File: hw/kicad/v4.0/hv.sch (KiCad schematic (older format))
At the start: 13 parts, among them P13 CONN_01X04, P2 CONN_01X02, U24 non_plated, U3 SI8621, U30 non_plated, U31 non_plated

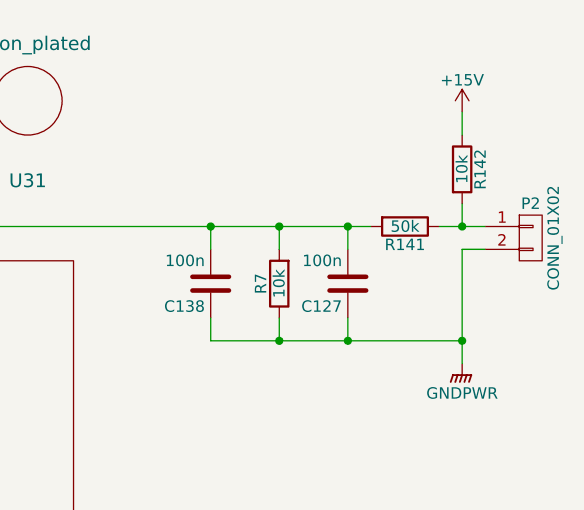
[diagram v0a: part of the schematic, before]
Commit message: v4.0 resistor values
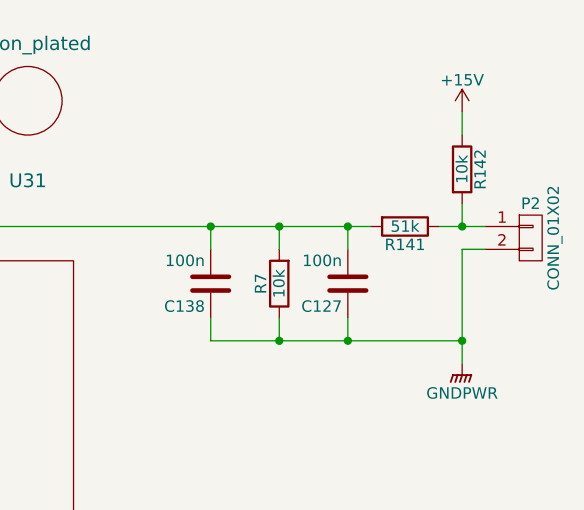
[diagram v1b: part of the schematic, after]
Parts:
- R141: value 50k -> 51k
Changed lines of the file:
@@
 P 9650 1650
 F 0 "R141" V 9730 1650 50  0000 C CNN
-F 1 "50k" V 9650 1650 50  0000 C CNN
+F 1 "51k" V 9650 1650 50  0000 C CNN
 F 2 "stmbl:R_0603" V 9580 1650 30  0001 C CNN
 F 3 "" H 9650 1650 30  0000 C CNN

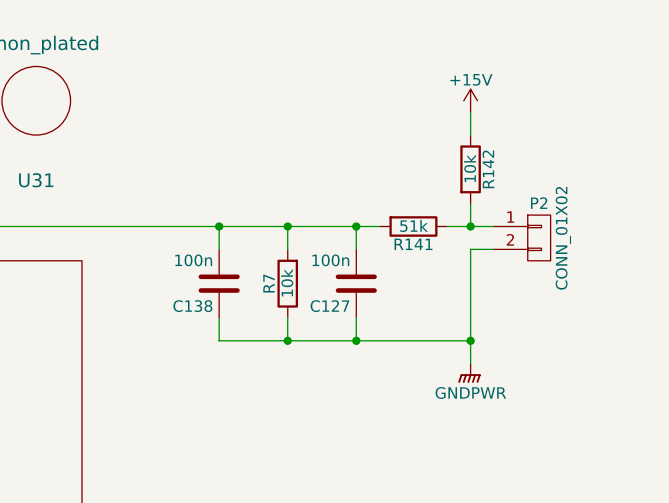
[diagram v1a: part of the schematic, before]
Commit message: v4.0 f3 ground, 15V DCDC
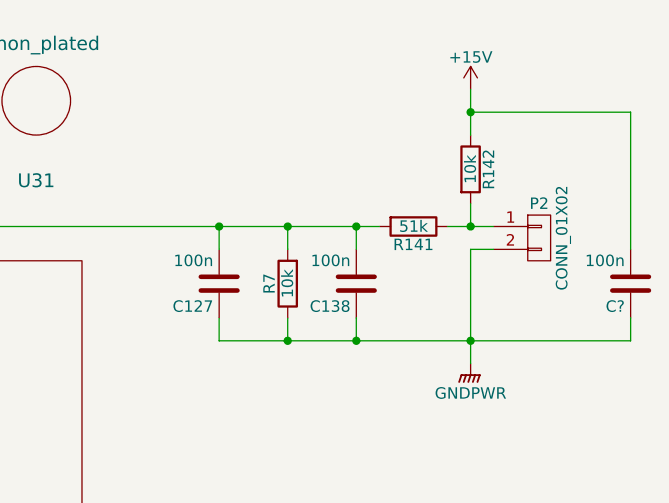
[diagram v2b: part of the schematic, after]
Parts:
- added C?: 100n, stmbl:C_0603, symbol C
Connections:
- net +15V: now also C?.2
- net GNDPWR: now also C?.1
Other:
- moved on the sheet: C127, C138
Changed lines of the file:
@@
 L +15V #PWR09
 U 1 1 57DCE570
-P 9900 1150
-F 0 "#PWR09" H 9900 1000 50  0001 C CNN
-F 1 "+15V" H 9900 1290 50  0000 C CNN
-F 2 "" H 9900 1150 50  0000 C CNN
-F 3 "" H 9900 1150 50  0000 C CNN
-	1    9900 1150
+P 9900 1050
+F 0 "#PWR09" H 9900 900 50  0001 C CNN
+F 1 "+15V" H 9900 1190 50  0000 C CNN
+F 2 "" H 9900 1050 50  0000 C CNN
+F 3 "" H 9900 1050 50  0000 C CNN
+	1    9900 1050
 	1    0    0    -1
 $EndComp
@@
 L C C127
 U 1 1 57DCE80A
-P 9400 1900
-F 0 "C127" H 9425 2000 50  0000 L CNN
-F 1 "100n" H 9425 1800 50  0000 L CNN
-F 2 "stmbl:C_0603" H 9438 1750 30  0001 C CNN
-F 3 "" H 9400 1900 60  0000 C CNN
-	1    9400 1900
+P 8800 1900
+F 0 "C127" H 8825 2000 50  0000 L CNN
+F 1 "100n" H 8825 1800 50  0000 L CNN
+F 2 "stmbl:C_0603" H 8838 1750 30  0001 C CNN
+F 3 "" H 8800 1900 60  0000 C CNN
+	1    8800 1900
 	-1   0    0    1
 $EndComp
@@
 	9100 2050 9100 2150
 Wire Wire Line
-	8800 2150 9900 2150
+	8800 2150 10600 2150
 Connection ~ 9900 2150
 Wire Wire Line
@@
 Connection ~ 9900 1650
 Wire Wire Line
-	9900 1150 9900 1250
+	9900 1050 9900 1250
 Wire Wire Line
 	6000 2250 5900 2250
@@
 L C C138
 U 1 1 58307AEE
-P 8800 1900
-F 0 "C138" H 8825 2000 50  0000 L CNN
-F 1 "100n" H 8825 1800 50  0000 L CNN
-F 2 "stmbl:C_0603" H 8838 1750 30  0001 C CNN
-F 3 "" H 8800 1900 60  0000 C CNN
-	1    8800 1900
+P 9400 1900
+F 0 "C138" H 9425 2000 50  0000 L CNN
+F 1 "100n" H 9425 1800 50  0000 L CNN
+F 2 "stmbl:C_0603" H 9438 1750 30  0001 C CNN
+F 3 "" H 9400 1900 60  0000 C CNN
+	1    9400 1900
 	-1   0    0    1
 $EndComp
@@
 Connection ~ 9100 2150
 NoConn ~ 7400 2800
+$Comp
+L C C?
+U 1 1 5886523B
+P 10600 1900
+F 0 "C?" H 10625 2000 50  0000 L CNN
+F 1 "100n" H 10625 1800 50  0000 L CNN
+F 2 "stmbl:C_0603" H 10638 1750 30  0001 C CNN
+F 3 "" H 10600 1900 60  0000 C CNN
+	1    10600 1900
+	-1   0    0    1
+$EndComp
+Wire Wire Line
+	9900 1150 10600 1150
+Wire Wire Line
+	10600 1150 10600 1750
+Connection ~ 9900 1150
+Wire Wire Line
+	10600 2150 10600 2050
 $EndSCHEMATC

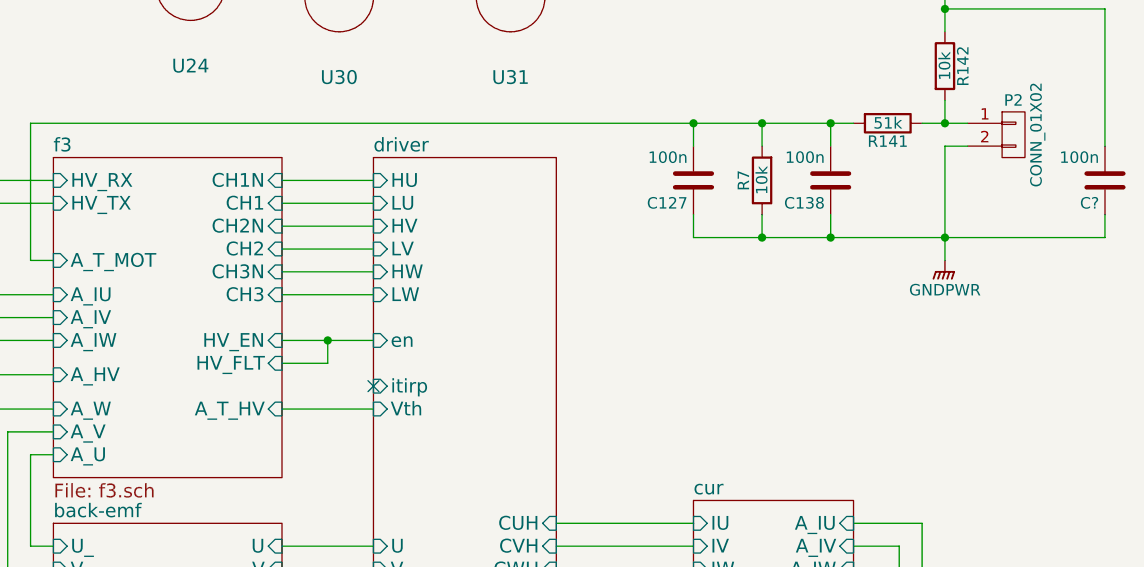
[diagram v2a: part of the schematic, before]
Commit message: v4.0 pwm fix
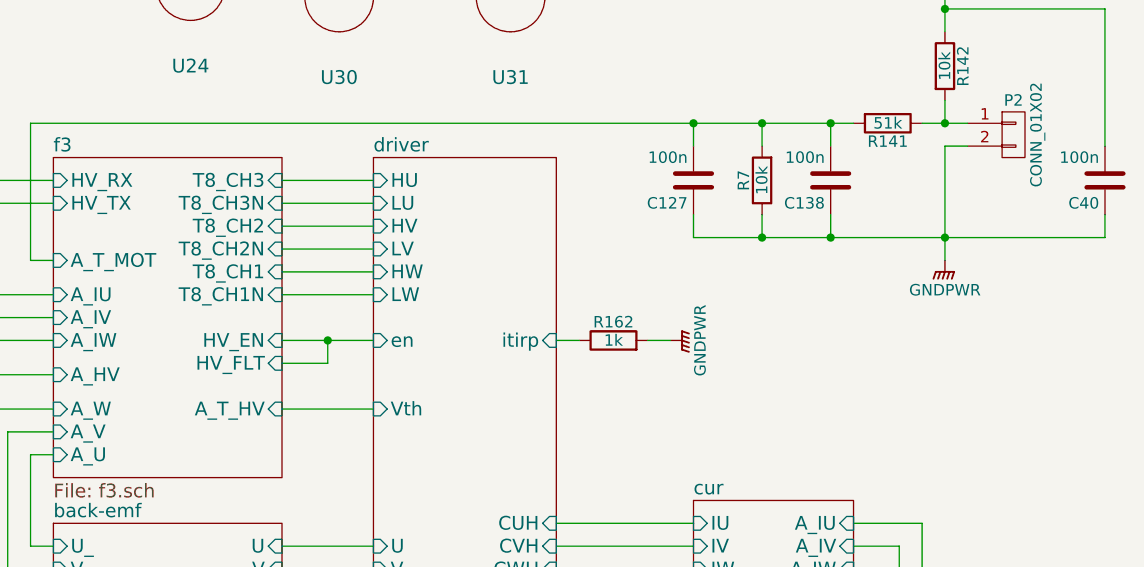
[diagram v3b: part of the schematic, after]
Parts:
- added R162: 1k, stmbl:R_0603, symbol R
- gave numbers to parts that had none: 1
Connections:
- net GNDPWR: now also R162.2
- net driver/itirp: now also R162.1
- no-connect marks 1 -> 0
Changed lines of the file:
@@
 F0 "f3" 60
 F1 "f3.sch" 60
-F2 "CH1N" I R 7000 1900 60
-F3 "CH2N" I R 7000 2100 60
-F4 "CH3N" I R 7000 2300 60
-F5 "CH1" I R 7000 2000 60
-F6 "CH2" I R 7000 2200 60
-F7 "CH3" I R 7000 2400 60
-F8 "HV_TX" I L 6000 2000 60
-F9 "HV_RX" I L 6000 1900 60
-F10 "A_HV" I L 6000 2750 60
-F11 "A_U" I L 6000 3100 60
-F12 "A_V" I L 6000 3000 60
-F13 "A_W" I L 6000 2900 60
-F14 "A_T_HV" I R 7000 2900 60
-F15 "HV_EN" I R 7000 2600 60
-F16 "HV_FLT" I R 7000 2700 60
-F17 "A_IU" I L 6000 2400 60
-F18 "A_IV" I L 6000 2500 60
-F19 "A_IW" I L 6000 2600 60
-F20 "A_T_MOT" I L 6000 2250 60
+F2 "HV_TX" I L 6000 2000 60
+F3 "HV_RX" I L 6000 1900 60
+F4 "A_HV" I L 6000 2750 60
+F5 "A_U" I L 6000 3100 60
+F6 "A_V" I L 6000 3000 60
+F7 "A_W" I L 6000 2900 60
+F8 "A_T_HV" I R 7000 2900 60
+F9 "HV_EN" I R 7000 2600 60
+F10 "HV_FLT" I R 7000 2700 60
+F11 "A_IU" I L 6000 2400 60
+F12 "A_IV" I L 6000 2500 60
+F13 "A_IW" I L 6000 2600 60
+F14 "A_T_MOT" I L 6000 2250 60
+F15 "T8_CH3" I R 7000 1900 60
+F16 "T8_CH2" I R 7000 2100 60
+F17 "T8_CH1" I R 7000 2300 60
+F18 "T8_CH3N" I R 7000 2000 60
+F19 "T8_CH2N" I R 7000 2200 60
+F20 "T8_CH1N" I R 7000 2400 60
 $EndSheet
 $Sheet
@@
 F11 "LW" I L 7400 2400 60
 F12 "en" I L 7400 2600 60
-F13 "itirp" I L 7400 2800 60
+F13 "itirp" I R 8200 2600 60
 F14 "CUH" I R 8200 3400 60
 F15 "CVH" I R 8200 3500 60
@@
 	8800 2050 8800 2150
 Connection ~ 9100 2150
-NoConn ~ 7400 2800
-$Comp
-L C C?
+$Comp
+L C C40
 U 1 1 5886523B
 P 10600 1900
-F 0 "C?" H 10625 2000 50  0000 L CNN
+F 0 "C40" H 10625 2000 50  0000 L CNN
 F 1 "100n" H 10625 1800 50  0000 L CNN
 F 2 "stmbl:C_0603" H 10638 1750 30  0001 C CNN
@@
 Wire Wire Line
 	10600 2150 10600 2050
+$Comp
+L R R162
+U 1 1 58871945
+P 8450 2600
+F 0 "R162" V 8530 2600 50  0000 C CNN
+F 1 "1k" V 8450 2600 50  0000 C CNN
+F 2 "stmbl:R_0603" V 8380 2600 30  0001 C CNN
+F 3 "" H 8450 2600 30  0000 C CNN
+	1    8450 2600
+	0    -1   -1   0
+$EndComp
+$Comp
+L GNDPWR #PWR011
+U 1 1 58871DBC
+P 8700 2600
+F 0 "#PWR011" H 8700 2400 50  0001 C CNN
+F 1 "GNDPWR" H 8700 2470 50  0000 C CNN
+F 2 "" H 8700 2550 60  0000 C CNN
+F 3 "" H 8700 2550 60  0000 C CNN
+	1    8700 2600
+	0    -1   -1   0
+$EndComp
+Wire Wire Line
+	8700 2600 8600 2600
+Wire Wire Line
+	8300 2600 8200 2600
 $EndSCHEMATC

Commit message: v4.1 fix
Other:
- note added: "<- do not populate"
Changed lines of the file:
@@
 Wire Wire Line
 	8300 2600 8200 2600
+Text Notes 2350 1500 1    60   ~ 0
+<- do not populate
 $EndSCHEMATC

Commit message: stmbl 4.2 wip
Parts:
- C127, C138, C19, C30, C40: symbol C -> stmbl1:C
- P13: symbol CONN_01X04 -> stmbl1:CONN_01X04
- P2: symbol CONN_01X02 -> stmbl1:CONN_01X02
- R141, R142, R162, R7: symbol R -> stmbl1:R
- U24, U30, U31: symbol non_plated -> stmbl1:non_plated
- U3: symbol SI8621 -> stmbl1:SI8621
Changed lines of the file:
@@
-EESchema Schematic File Version 2
-LIBS:transistors
-LIBS:stm32
-LIBS:conn
-LIBS:power
-LIBS:74xgxx
-LIBS:74xx
-LIBS:ac-dc
-LIBS:actel
-LIBS:adc-dac
-LIBS:Altera
-LIBS:analog_devices
-LIBS:analog_switches
-LIBS:atmel
-LIBS:audio
-LIBS:brooktre
-LIBS:cmos_ieee
-LIBS:cmos4000
-LIBS:contrib
-LIBS:cypress
-LIBS:dc-dc
-LIBS:device
-LIBS:digital-audio
-LIBS:diode
-LIBS:display
-LIBS:dsp
-LIBS:elec-unifil
-LIBS:ESD_Protection
-LIBS:ftdi
-LIBS:gennum
-LIBS:graphic
-LIBS:hc11
-LIBS:intel
-LIBS:interface
-LIBS:ir
-LIBS:Lattice
-LIBS:linear
-LIBS:logo
-LIBS:maxim
-LIBS:memory
-LIBS:microchip_dspic33dsc
-LIBS:microchip_pic10mcu
-LIBS:microchip_pic12mcu
-LIBS:microchip_pic16mcu
-LIBS:microchip_pic18mcu
-LIBS:microchip_pic32mcu
-LIBS:microchip
-LIBS:microcontrollers
-LIBS:motor_drivers
-LIBS:motorola
-LIBS:msp430
-LIBS:nordicsemi
-LIBS:nxp_armmcu
-LIBS:onsemi
-LIBS:opto
-LIBS:Oscillators
-LIBS:philips
-LIBS:Power_Management
-LIBS:powerint
-LIBS:pspice
-LIBS:references
-LIBS:regul
-LIBS:relays
-LIBS:rfcom
-LIBS:sensors
-LIBS:silabs
-LIBS:siliconi
-LIBS:stm8
-LIBS:supertex
-LIBS:switches
-LIBS:texas
-LIBS:transf
-LIBS:ttl_ieee
-LIBS:valves
-LIBS:video
-LIBS:Xicor
-LIBS:xilinx
-LIBS:Zilog
+EESchema Schematic File Version 4
 LIBS:stmbl_4.0-cache
-EELAYER 25 0
+EELAYER 26 0
 EELAYER END
 $Descr A4 11693 8268
@@
 $EndDescr
 $Comp
-L SI8621 U3
+L stmbl1:SI8621 U3
 U 1 1 56590991
 P 4050 1950
@@
 RX
 $Comp
-L GND #PWR01
+L stmbl1:GND #PWR01
 U 1 1 566A2E2E
 P 3700 2800
@@
 $EndComp
 $Comp
-L GNDPWR #PWR02
+L stmbl1:GNDPWR #PWR02
 U 1 1 566A2FC8
 P 4400 2800
@@
 $EndComp
 $Comp
-L +3.3V #PWR03
+L stmbl1:+3.3V #PWR03
 U 1 1 566A3162
 P 3700 1050
@@
 $EndComp
 $Comp
-L +3.3VP #PWR04
+L stmbl1:+3.3VP #PWR04
 U 1 1 566A32FC
 P 4400 1050
@@
 $EndComp
 $Comp
-L C C19
+L stmbl1:C C19
 U 1 1 566A3B64
 P 3450 1150
@@
 $EndComp
 $Comp
-L C C30
+L stmbl1:C C30
 U 1 1 566A4471
 P 4650 1150
@@
 $EndComp
 $Comp
-L GND #PWR05
+L stmbl1:GND #PWR05
 U 1 1 566A4897
 P 3200 1150
@@
 $EndComp
 $Comp
-L GNDPWR #PWR06
+L stmbl1:GNDPWR #PWR06
 U 1 1 566A4A42
 P 4900 1150
@@
 RX
 $Comp
-L +3.3V #PWR07
+L stmbl1:+3.3V #PWR07
 U 1 1 5784C75E
 P 2550 1550
@@
 $EndComp
 $Comp
-L GND #PWR08
+L stmbl1:GND #PWR08
 U 1 1 5784C766
 P 2550 1950
@@
 $EndComp
 $Comp
-L CONN_01X04 P13
+L stmbl1:CONN_01X04 P13
 U 1 1 57AEC939
 P 2300 1750
@@
 $EndComp
 $Comp
-L CONN_01X02 P2
+L stmbl1:CONN_01X02 P2
 U 1 1 57DC49A6
 P 10200 1700
@@
 $EndComp
 $Comp
-L +15V #PWR09
+L stmbl1:+15V #PWR09
 U 1 1 57DCE570
 P 9900 1050
@@
 $EndComp
 $Comp
-L R R142
+L stmbl1:R R142
 U 1 1 57DCE6B7
 P 9900 1400
@@
 $EndComp
 $Comp
-L C C127
+L stmbl1:C C127
 U 1 1 57DCE80A
 P 8800 1900
@@
 $EndComp
 $Comp
-L R R141
+L stmbl1:R R141
 U 1 1 57DD09BB
 P 9650 1650
@@
 $EndComp
 $Comp
-L R R7
+L stmbl1:R R7
 U 1 1 57DD2315
 P 9100 1900
@@
 $EndComp
 $Comp
-L GNDPWR #PWR010
+L stmbl1:GNDPWR #PWR010
 U 1 1 57DD49BF
 P 9900 2250
@@
 	7000 2400 7400 2400
 Wire Wire Line
-	7000 2600 7400 2600
+	7000 2600 7200 2600
 Wire Wire Line
 	7000 2700 7200 2700
@@
 	5550 2750 6000 2750
 Wire Wire Line
-	4400 1050 4400 1250
-Wire Wire Line
-	3700 1050 3700 1250
+	4400 1050 4400 1150
+Wire Wire Line
+	3700 1050 3700 1150
 Wire Wire Line
 	3100 1800 3200 1800
@@
 	10000 1750 9900 1750
 Wire Wire Line
-	9900 1750 9900 2250
+	9900 1750 9900 2150
 Wire Wire Line
 	9100 2050 9100 2150
 Wire Wire Line
-	8800 2150 10600 2150
+	8800 2150 9100 2150
 Connection ~ 9900 2150
 Wire Wire Line
@@
 Connection ~ 9400 2150
 Wire Wire Line
-	5900 1650 9500 1650
+	5900 1650 8800 1650
 Wire Wire Line
 	9400 1650 9400 1750
@@
 Connection ~ 9400 1650
 Wire Wire Line
-	9800 1650 10000 1650
+	9800 1650 9900 1650
 Wire Wire Line
 	9900 1550 9900 1650
 Connection ~ 9900 1650
 Wire Wire Line
-	9900 1050 9900 1250
+	9900 1050 9900 1150
 Wire Wire Line
 	6000 2250 5900 2250
@@
 	5400 1800 5400 1900
 $Comp
-L non_plated U24
+L stmbl1:non_plated U24
 U 1 1 58275572
 P 6600 1050
@@
 $EndComp
 $Comp
-L non_plated U30
+L stmbl1:non_plated U30
 U 1 1 582756C2
 P 7250 1100
@@
 $EndComp
 $Comp
-L non_plated U31
+L stmbl1:non_plated U31
 U 1 1 58275820
 P 8000 1100
@@
 $EndComp
 $Comp
-L C C138
+L stmbl1:C C138
 U 1 1 58307AEE
 P 9400 1900
@@
 Connection ~ 9100 2150
 $Comp
-L C C40
+L stmbl1:C C40
 U 1 1 5886523B
 P 10600 1900
@@
 	10600 2150 10600 2050
 $Comp
-L R R162
+L stmbl1:R R162
 U 1 1 58871945
 P 8450 2600
@@
 $EndComp
 $Comp
-L GNDPWR #PWR011
+L stmbl1:GNDPWR #PWR011
 U 1 1 58871DBC
 P 8700 2600
@@
 Text Notes 2350 1500 1    60   ~ 0
 <- do not populate
+Wire Wire Line
+	7200 2600 7400 2600
+Wire Wire Line
+	3700 1150 3700 1250
+Wire Wire Line
+	4400 1150 4400 1250
+Wire Wire Line
+	9900 2150 9900 2250
+Wire Wire Line
+	9900 2150 10600 2150
+Wire Wire Line
+	9400 2150 9900 2150
+Wire Wire Line
+	9400 1650 9500 1650
+Wire Wire Line
+	9900 1650 10000 1650
+Wire Wire Line
+	9100 1650 9400 1650
+Wire Wire Line
+	8800 1650 9100 1650
+Wire Wire Line
+	9100 2150 9400 2150
+Wire Wire Line
+	9900 1150 9900 1250
 $EndSCHEMATC

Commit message: stmbl 4.2
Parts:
- P13: footprint Socket_Strips:Socket_Strip_Straight_1x04 -> stmbl:Socket_Strip_Straight_1x04
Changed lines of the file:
@@
 F 0 "P13" H 2300 2000 50  0000 C CNN
 F 1 "CONN_01X04" V 2400 1750 50  0000 C CNN
-F 2 "Socket_Strips:Socket_Strip_Straight_1x04" H 2300 1750 50  0001 C CNN
+F 2 "stmbl:Socket_Strip_Straight_1x04" H 2300 1750 50  0001 C CNN
 F 3 "" H 2300 1750 50  0000 C CNN
 	1    2300 1750

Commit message: stmbl 4.2 bom
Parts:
- C127, C138, C19, C30, C40: Manufacturer No (none) -> (none); Source (none) -> (none); Tolerance (none) -> X7R; Voltage (none) -> 50V
- P2: Manufacturer No (none) -> Phoenix 1844210; Source (none) -> (none); Tolerance (none) -> (none); Voltage (none) -> (none)
- R141: Manufacturer No (none) -> (none); Source (none) -> (none); Tolerance (none) -> 1%
- R142, R162, R7: Manufacturer No (none) -> (none); Source (none) -> (none); Tolerance (none) -> 1%; Voltage (none) -> (none)
- U3: Manufacturer No (none) -> Si8621BB-B-IS; Source (none) -> (none); Voltage (none) -> (none)
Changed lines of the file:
@@
 F 2 "stmbl:SOIC-8-N" H 4050 1950 60  0001 C CNN
 F 3 "" H 4050 1950 60  0000 C CNN
+F 4 "Si8621BB-B-IS" H 4050 1950 50  0001 C CNN "Manufacturer No"
+F 5 " " H 4050 1950 50  0001 C CNN "Voltage"
+F 6 " " H 4050 1950 50  0001 C CNN "Source"
 	1    4050 1950
 	1    0    0    -1
@@
 F 2 "stmbl:C_0603" H 3488 1000 30  0001 C CNN
 F 3 "" H 3450 1150 60  0000 C CNN
+F 4 " " H 3450 1150 50  0001 C CNN "Manufacturer No"
+F 5 "50V" H 3450 1150 50  0001 C CNN "Voltage"
+F 6 " " H 3450 1150 50  0001 C CNN "Source"
+F 7 "X7R" H 3450 1150 50  0001 C CNN "Tolerance"
 	1    3450 1150
 	0    1    1    0
@@
 F 2 "stmbl:C_0603" H 4688 1000 30  0001 C CNN
 F 3 "" H 4650 1150 60  0000 C CNN
+F 4 " " H 4650 1150 50  0001 C CNN "Manufacturer No"
+F 5 "50V" H 4650 1150 50  0001 C CNN "Voltage"
+F 6 " " H 4650 1150 50  0001 C CNN "Source"
+F 7 "X7R" H 4650 1150 50  0001 C CNN "Tolerance"
 	1    4650 1150
 	0    1    1    0
@@
 F 2 "stmbl:akl182-2" H 10200 1700 50  0001 C CNN
 F 3 "" H 10200 1700 50  0000 C CNN
+F 4 "Phoenix 1844210" H 10200 1700 50  0001 C CNN "Manufacturer No"
+F 5 " " H 10200 1700 50  0001 C CNN "Voltage"
+F 6 " " H 10200 1700 50  0001 C CNN "Source"
+F 7 " " H 10200 1700 50  0001 C CNN "Tolerance"
 	1    10200 1700
 	1    0    0    -1
@@
 F 2 "stmbl:R_0603" V 9830 1400 30  0001 C CNN
 F 3 "" H 9900 1400 30  0000 C CNN
+F 4 " " H 9900 1400 50  0001 C CNN "Manufacturer No"
+F 5 " " H 9900 1400 50  0001 C CNN "Voltage"
+F 6 " " H 9900 1400 50  0001 C CNN "Source"
+F 7 "1%" H 9900 1400 50  0001 C CNN "Tolerance"
 	1    9900 1400
 	1    0    0    -1
@@
 F 2 "stmbl:C_0603" H 8838 1750 30  0001 C CNN
 F 3 "" H 8800 1900 60  0000 C CNN
+F 4 " " H 8800 1900 50  0001 C CNN "Manufacturer No"
+F 5 "50V" H 8800 1900 50  0001 C CNN "Voltage"
+F 6 " " H 8800 1900 50  0001 C CNN "Source"
+F 7 "X7R" H 8800 1900 50  0001 C CNN "Tolerance"
 	1    8800 1900
 	-1   0    0    1
@@
 F 2 "stmbl:R_0603" V 9580 1650 30  0001 C CNN
 F 3 "" H 9650 1650 30  0000 C CNN
+F 4 " " H 9650 1650 50  0001 C CNN "Manufacturer No"
+F 5 " " H 9650 1650 50  0001 C CNN "Source"
+F 6 "1%" H 9650 1650 50  0001 C CNN "Tolerance"
 	1    9650 1650
 	0    1    1    0
@@
 F 2 "stmbl:R_0603" V 9030 1900 30  0001 C CNN
 F 3 "" H 9100 1900 30  0000 C CNN
+F 4 " " H 9100 1900 50  0001 C CNN "Manufacturer No"
+F 5 " " H 9100 1900 50  0001 C CNN "Voltage"
+F 6 " " H 9100 1900 50  0001 C CNN "Source"
+F 7 "1%" H 9100 1900 50  0001 C CNN "Tolerance"
 	1    9100 1900
 	-1   0    0    1
@@
 F 2 "stmbl:C_0603" H 9438 1750 30  0001 C CNN
 F 3 "" H 9400 1900 60  0000 C CNN
+F 4 " " H 9400 1900 50  0001 C CNN "Manufacturer No"
+F 5 "50V" H 9400 1900 50  0001 C CNN "Voltage"
+F 6 " " H 9400 1900 50  0001 C CNN "Source"
+F 7 "X7R" H 9400 1900 50  0001 C CNN "Tolerance"
 	1    9400 1900
 	-1   0    0    1
@@
 F 2 "stmbl:C_0603" H 10638 1750 30  0001 C CNN
 F 3 "" H 10600 1900 60  0000 C CNN
+F 4 " " H 10600 1900 50  0001 C CNN "Manufacturer No"
+F 5 "50V" H 10600 1900 50  0001 C CNN "Voltage"
+F 6 " " H 10600 1900 50  0001 C CNN "Source"
+F 7 "X7R" H 10600 1900 50  0001 C CNN "Tolerance"
 	1    10600 1900
 	-1   0    0    1
@@
 F 2 "stmbl:R_0603" V 8380 2600 30  0001 C CNN
 F 3 "" H 8450 2600 30  0000 C CNN
+F 4 " " H 8450 2600 50  0001 C CNN "Manufacturer No"
+F 5 " " H 8450 2600 50  0001 C CNN "Voltage"
+F 6 " " H 8450 2600 50  0001 C CNN "Source"
+F 7 "1%" H 8450 2600 50  0001 C CNN "Tolerance"
 	1    8450 2600
 	0    -1   -1   0

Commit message: stmbl 4.2 lib fix
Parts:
- C127, C138, C19, C30, C40: symbol stmbl1:C -> stmbl:C
- P13: symbol stmbl1:CONN_01X04 -> stmbl:CONN_01X04
- P2: symbol stmbl1:CONN_01X02 -> stmbl:CONN_01X02
- R141, R142, R162, R7: symbol stmbl1:R -> stmbl:R
- U24, U30, U31: symbol stmbl1:non_plated -> stmbl:non_plated
- U3: symbol stmbl1:SI8621 -> stmbl:SI8621
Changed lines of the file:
@@
 $EndDescr
 $Comp
-L stmbl1:SI8621 U3
+L stmbl:SI8621 U3
 U 1 1 56590991
 P 4050 1950
@@
 RX
 $Comp
-L stmbl1:GND #PWR01
+L stmbl:GND #PWR01
 U 1 1 566A2E2E
 P 3700 2800
@@
 $EndComp
 $Comp
-L stmbl1:GNDPWR #PWR02
+L stmbl:GNDPWR #PWR02
 U 1 1 566A2FC8
 P 4400 2800
@@
 $EndComp
 $Comp
-L stmbl1:+3.3V #PWR03
+L stmbl:+3.3V #PWR03
 U 1 1 566A3162
 P 3700 1050
@@
 $EndComp
 $Comp
-L stmbl1:+3.3VP #PWR04
+L stmbl:+3.3VP #PWR04
 U 1 1 566A32FC
 P 4400 1050
@@
 $EndComp
 $Comp
-L stmbl1:C C19
+L stmbl:C C19
 U 1 1 566A3B64
 P 3450 1150
@@
 $EndComp
 $Comp
-L stmbl1:C C30
+L stmbl:C C30
 U 1 1 566A4471
 P 4650 1150
@@
 $EndComp
 $Comp
-L stmbl1:GND #PWR05
+L stmbl:GND #PWR05
 U 1 1 566A4897
 P 3200 1150
@@
 $EndComp
 $Comp
-L stmbl1:GNDPWR #PWR06
+L stmbl:GNDPWR #PWR06
 U 1 1 566A4A42
 P 4900 1150
@@
 RX
 $Comp
-L stmbl1:+3.3V #PWR07
+L stmbl:+3.3V #PWR07
 U 1 1 5784C75E
 P 2550 1550
@@
 $EndComp
 $Comp
-L stmbl1:GND #PWR08
+L stmbl:GND #PWR08
 U 1 1 5784C766
 P 2550 1950
@@
 $EndComp
 $Comp
-L stmbl1:CONN_01X04 P13
+L stmbl:CONN_01X04 P13
 U 1 1 57AEC939
 P 2300 1750
@@
 $EndComp
 $Comp
-L stmbl1:CONN_01X02 P2
+L stmbl:CONN_01X02 P2
 U 1 1 57DC49A6
 P 10200 1700
@@
 $EndComp
 $Comp
-L stmbl1:+15V #PWR09
+L stmbl:+15V #PWR09
 U 1 1 57DCE570
 P 9900 1050
@@
 $EndComp
 $Comp
-L stmbl1:R R142
+L stmbl:R R142
 U 1 1 57DCE6B7
 P 9900 1400
@@
 $EndComp
 $Comp
-L stmbl1:C C127
+L stmbl:C C127
 U 1 1 57DCE80A
 P 8800 1900
@@
 $EndComp
 $Comp
-L stmbl1:R R141
+L stmbl:R R141
 U 1 1 57DD09BB
 P 9650 1650
@@
 $EndComp
 $Comp
-L stmbl1:R R7
+L stmbl:R R7
 U 1 1 57DD2315
 P 9100 1900
@@
 $EndComp
 $Comp
-L stmbl1:GNDPWR #PWR010
+L stmbl:GNDPWR #PWR010
 U 1 1 57DD49BF
 P 9900 2250
@@
 	5400 1800 5400 1900
 $Comp
-L stmbl1:non_plated U24
+L stmbl:non_plated U24
 U 1 1 58275572
 P 6600 1050
@@
 $EndComp
 $Comp
-L stmbl1:non_plated U30
+L stmbl:non_plated U30
 U 1 1 582756C2
 P 7250 1100
@@
 $EndComp
 $Comp
-L stmbl1:non_plated U31
+L stmbl:non_plated U31
 U 1 1 58275820
 P 8000 1100
@@
 $EndComp
 $Comp
-L stmbl1:C C138
+L stmbl:C C138
 U 1 1 58307AEE
 P 9400 1900
@@
 Connection ~ 9100 2150
 $Comp
-L stmbl1:C C40
+L stmbl:C C40
 U 1 1 5886523B
 P 10600 1900
@@
 	10600 2150 10600 2050
 $Comp
-L stmbl1:R R162
+L stmbl:R R162
 U 1 1 58871945
 P 8450 2600
@@
 $EndComp
 $Comp
-L stmbl1:GNDPWR #PWR011
+L stmbl:GNDPWR #PWR011
 U 1 1 58871DBC
 P 8700 2600
